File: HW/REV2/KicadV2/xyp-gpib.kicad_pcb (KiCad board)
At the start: 2 copper layers, 54 x 15 mm, 25 parts, among them J1 USB_C_Receptacle_USB2.0, SW1 SW_Push, U1 ATmega32U4-MU, Y1 CX2016DB16000D0WZRC1

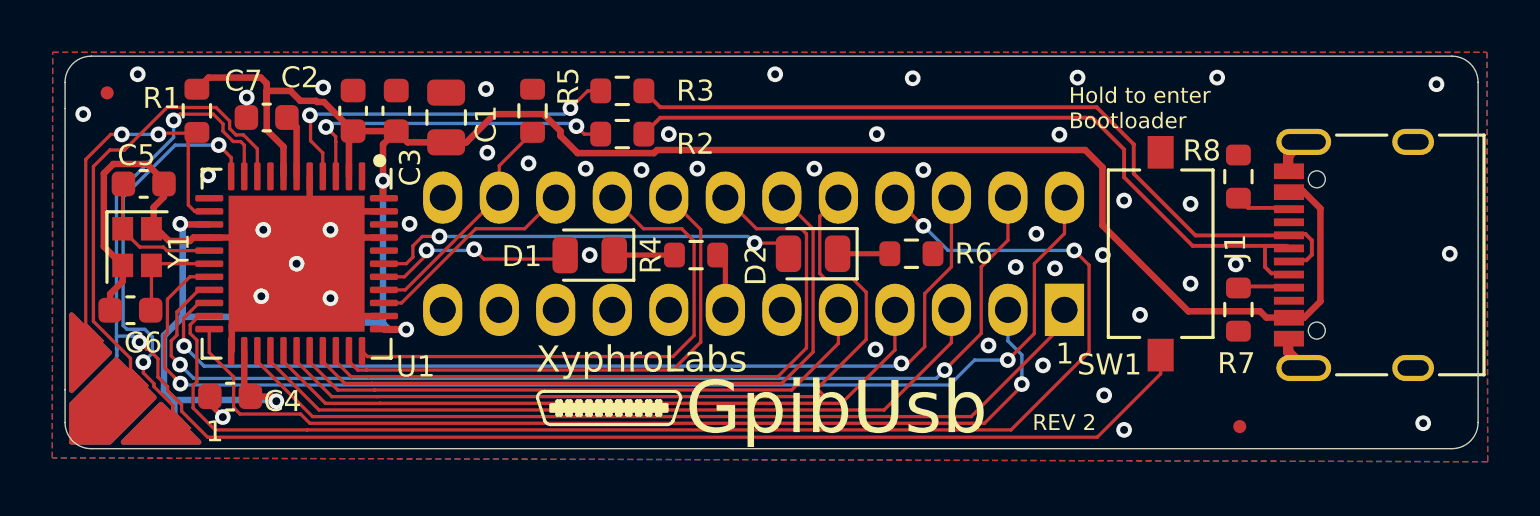
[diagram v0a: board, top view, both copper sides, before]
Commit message: [MOD] Re-route with proper rules and USBLC6-2P6
Signed-off-by: Silvano Cortesi <silvano.cortesi@hotmail.com>
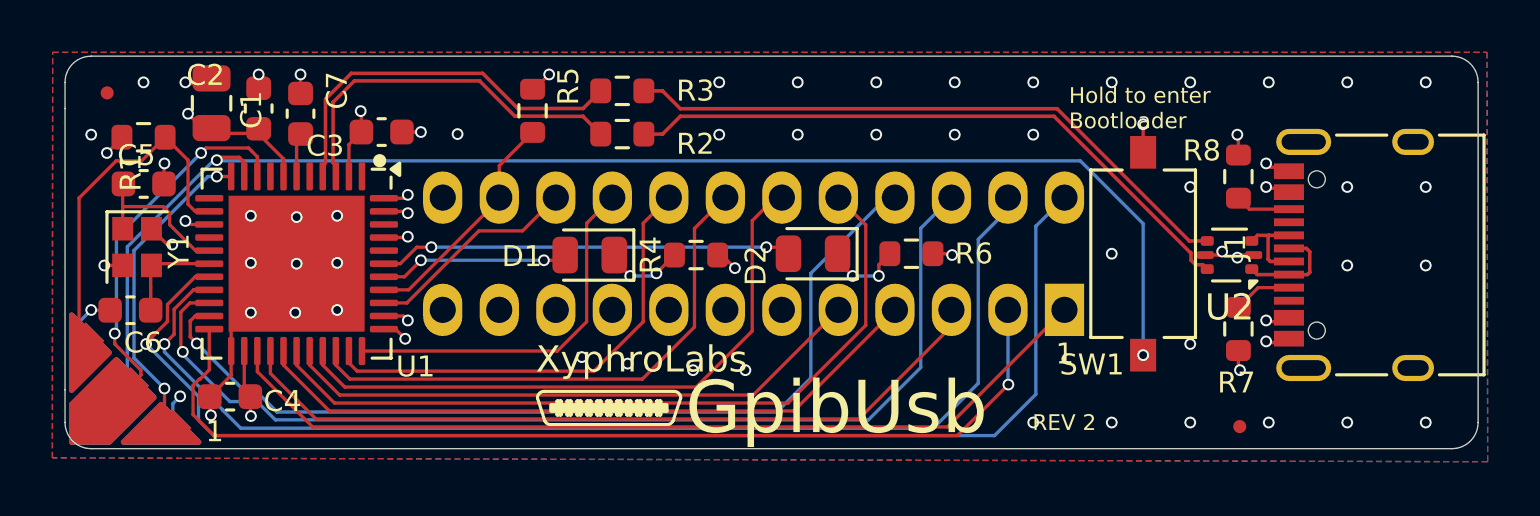
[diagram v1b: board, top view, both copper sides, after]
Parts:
- added U2: USBLC6-2P6, Package_TO_SOT_SMD:SOT-666, F.Cu at (224.5, 82.6)
- GPIB1: value 112-024-113R001 -> 111-024-113L001; footprint gpib:112024113R001 -> usbgpib-footprints:GPIB
- ISP1: footprint Kai:EdgeProg -> usbgpib-footprints:EdgeProg-ISP
- R7: value 10k -> 5k1
- moved C1 8.98 mm to (185.6, 76.8)
- moved C2 3.61 mm to (187.4, 77.0)
- moved R1 2.28 mm to (183.0, 78.1), turned to 0 degrees
- moved C7 1.30 mm to (189.0, 77.2), turned to 90 degrees
- moved C3 0.98 mm to (192.1, 77.9), turned to 0 degrees
- moved R7 0.74 mm to (224.8, 85.4)
- moved SW1 0.67 mm to (221.2, 82.5)
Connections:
- net Net-(U1-D+) renamed /MCU_D+
- net Net-(U1-D-) renamed /MCU_D-
- J1 pad A6: /D+ -> /USB_D+
- J1 pad A7: /D- -> /USB_D-
- J1 pad B6: /D+ -> /USB_D+
- J1 pad B7: /D- -> /USB_D-
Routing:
- net +5V: track 94.8 -> 18.1 mm, vias 4 -> 11
- net GND: track 32.4 -> 52.8 mm, vias 45 -> 65
- net /DIO4: track 51.8 -> 35.3 mm, vias 2 -> 1
- net /MOSI: track 60.1 -> 53.3 mm
- net /IFC: track 21.0 -> 14.2 mm
- net /NRFD: track 27.1 -> 20.7 mm
- net /D+: track 30.1 -> 23.9 mm
- net /D-: track 30.2 -> 24.4 mm
- net /SCK: track 18.0 -> 14.0 mm, vias 0 -> 2
- net /USB_D-: track 0.00 -> 3.98 mm
- net /MISO: track 16.2 -> 12.3 mm
- net /DIO1: track 44.6 -> 48.5 mm, vias 2 -> 1
- net /USB_D+: track 0.00 -> 3.27 mm
- net /DIO2: track 41.0 -> 44.0 mm, vias 2 -> 1
- net /NDAC: track 20.4 -> 17.8 mm
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- added copper zone on In2.Cu, net +5V
- added copper zone on In1.Cu, net GND
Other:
- copper layers 2 -> 4

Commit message: [ADD] Fabrication output and Rev. 2.1
Signed-off-by: Silvano Cortesi <silvano.cortesi@hotmail.com>
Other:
- board text added: "REV 2.1"
- board text removed: "REV 2"
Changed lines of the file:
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@@
 		(tenting front back)
 		(pcbplotparams
-			(layerselection 0x00000000_00000000_55555555_5755f5ff)
+			(layerselection 0x00000000_00000000_55555555_575575ff)
 			(plot_on_all_layers_selection 0x00000000_00000000_00000000_00000000)
 			(disableapertmacros no)
@@
 			(drillshape 0)
 			(scaleselection 1)
-			(outputdirectory "gerbers/")
+			(outputdirectory "../Gerber filesV2/")
 		)
 	)
@@
 			(at -0.254 1.524 270)
 			(layer "F.SilkS")
+			(hide yes)
 			(effects
 				(font
@@
 			(at 1.27 -2.032 0)
 			(layer "F.SilkS")
+			(hide yes)
 			(effects
 				(font
@@
 			(at 0.889 1.397 90)
 			(layer "F.SilkS")
+			(hide yes)
 			(effects
 				(font
@@
 			(at 2.5908 -0.0508 0)
 			(layer "F.SilkS")
+			(hide yes)
 			(effects
 				(font
@@
 			(at -0.4826 1.3462 90)
 			(layer "F.SilkS")
+			(hide yes)
 			(effects
 				(font
@@
 			(at 2.794 0.381 180)
 			(layer "F.SilkS")
+			(hide yes)
 			(effects
 				(font
@@
 			(at 2.794 0 180)
 			(layer "F.SilkS")
+			(hide yes)
 			(effects
 				(font
@@
 			(at -1.7272 0 90)
 			(layer "F.SilkS")
+			(hide yes)
 			(effects
 				(font
@@
 			(at 0.9398 1.3716 270)
 			(layer "F.SilkS")
+			(hide yes)
 			(effects
 				(font
@@
 			(at 3.937 -4.5466 0)
 			(layer "F.SilkS")
+			(hide yes)
 			(effects
 				(font
@@
 			(at -0.2794 -1.0922 0)
 			(layer "F.SilkS")
+			(hide yes)
 			(effects
 				(font
@@
 			(at -0.4826 -1.2446 0)
 			(layer "F.SilkS")
+			(hide yes)
 			(effects
 				(font
@@
 			(at 0.1524 -1.6002 90)
 			(layer "F.SilkS")
+			(hide yes)
 			(effects
 				(font
@@
 			(at -2.159 0.5334 0)
 			(layer "F.SilkS")
+			(hide yes)
 			(effects
 				(font
@@
 			(at -2.0066 -0.1778 180)
 			(layer "F.SilkS")
+			(hide yes)
 			(effects
 				(font
@@
 			(at 0 -2 0)
 			(layer "F.SilkS")
+			(hide yes)
 			(effects
 				(font
@@
 			(at 0.3008 -5.715 90)
 			(layer "F.SilkS")
+			(hide yes)
 			(effects
 				(font
@@
 			(at 2.3876 0 0)
 			(layer "F.SilkS")
+			(hide yes)
 			(effects
 				(font
@@
 			(at 2.1844 -0.4572 90)
 			(layer "F.SilkS")
+			(hide yes)
 			(effects
 				(font
@@
 			(unlocked yes)
 			(layer "F.SilkS")
+			(hide yes)
 			(effects
 				(font
@@
 			(at 2.0574 0.0762 0)
 			(layer "F.SilkS")
+			(hide yes)
 			(effects
 				(font
@@
 			(at -0.9906 1.397 0)
 			(layer "F.SilkS")
+			(hide yes)
 			(effects
 				(font
@@
 		)
 	)
-	(gr_text "REV 2"
+	(gr_text "REV 2.1"
 		(at 216.9668 89.3572 0)
 		(layer "F.SilkS")
@@
 			(justify left bottom)
 		)
-		(render_cache "REV 2" 0
+		(render_cache "REV 2.1" 0
 			(polygon
 				(pts
@@
 				)
 			)
+			(polygon
+				(pts
+					(xy 219.769156 89.088724) (xy 219.947466 89.088724) (xy 219.947466 89.2552) (xy 219.769156 89.2552)
+				)
+			)
+			(polygon
+				(pts
+					(xy 220.410697 88.645569) (xy 220.410697 89.2552) (xy 220.24184 89.2552) (xy 220.24184 88.856632)
+					(xy 220.200569 88.885225) (xy 220.162522 88.906714) (xy 220.12148 88.92461) (xy 220.066388 88.94335)
+					(xy 220.066388 88.807356) (xy 220.122312 88.786283) (xy 220.165748 88.764089) (xy 220.198792 88.741081)
+					(xy 220.22787 88.713359) (xy 220.252398 88.681653) (xy 220.272578 88.645569)
+				)
+			)
